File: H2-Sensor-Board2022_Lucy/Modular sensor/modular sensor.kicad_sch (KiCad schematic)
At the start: 5 parts, among them J1 Conn_01x03_Pin

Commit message: Started Layout fixed footprint for daughter baord and added M3 mounting holes.
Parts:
- H1: footprint MountingHole:MountingHole_2.7mm_M2.5_Pad_Via -> MountingHole:MountingHole_3.2mm_M3_Pad
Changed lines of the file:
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@@
       (effects (font (size 1.27 1.27)) (justify right))
     )
-    (property "Footprint" "MountingHole:MountingHole_2.7mm_M2.5_Pad_Via" (at 148.59 118.11 0)
+    (property "Footprint" "MountingHole:MountingHole_3.2mm_M3_Pad" (at 148.59 118.11 0)
       (effects (font (size 1.27 1.27)) hide)
     )

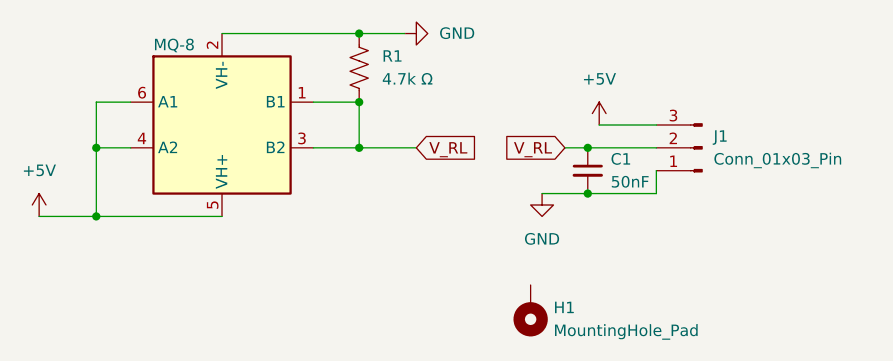
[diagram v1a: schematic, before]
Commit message: Added all required components made modular sensor smaller and and laid out main board
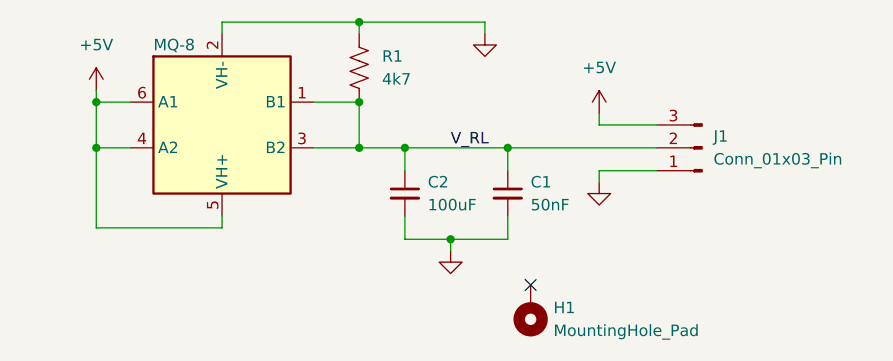
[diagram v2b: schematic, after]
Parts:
- added C2: 100uF, Capacitor_SMD:C_1206_3216Metric_Pad1.33x1.80mm_HandSolder, symbol Device:C_Small
- R1: value 4.7k Ω -> 4k7
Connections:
- net GND: now also C2.2
- net V_RL: now also C2.1
- no-connect marks 0 -> 1
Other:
- moved on the sheet: C1

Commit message: I am highly sleep deprived
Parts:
- removed C1: 50nF, Capacitor_SMD:C_1206_3216Metric_Pad1.33x1.80mm_HandSolder, symbol Device:C_Small
- removed C2: 100uF, Capacitor_SMD:C_1206_3216Metric_Pad1.33x1.80mm_HandSolder, symbol Device:C_Small
- removed R1: 4k7, Resistor_SMD:R_1206_3216Metric_Pad1.30x1.75mm_HandSolder, symbol Device:R_US
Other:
- moved on the sheet: J1
